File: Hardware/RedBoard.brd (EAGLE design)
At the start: 68.6 x 53.3 mm, 75 parts, among them IC3 LM1117, J1 AMP FCI 10103594-0001LF, J2 ISP, J3 POWER_JACKSUPER_BOMB_DIGITY, Q1 1A/60V/500mΩ, Q2 2N7002PW, Q3 2N7002PW, U1 CH340C, U3 AP2112-3.3V, U4 ATMEGA328P_TQFP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

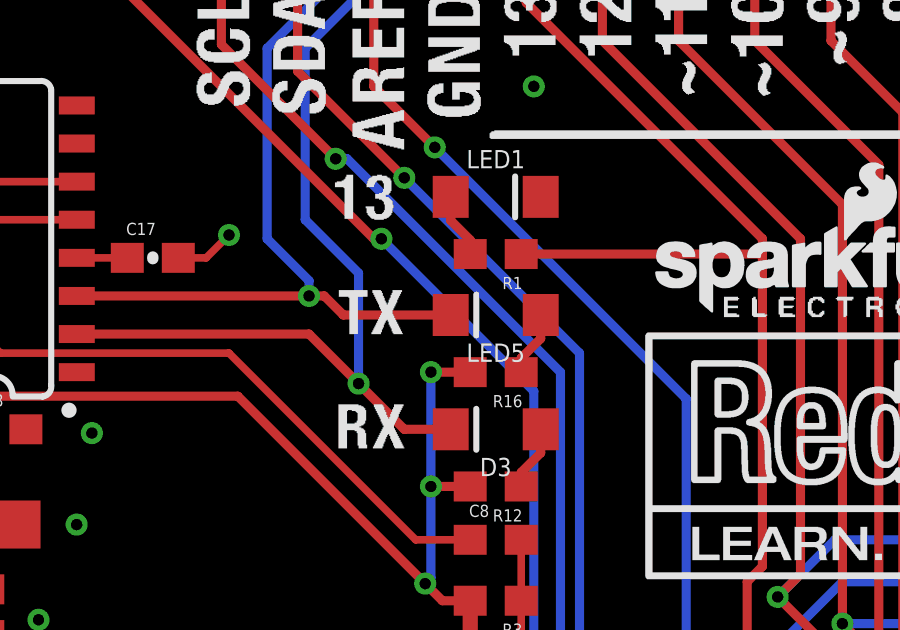
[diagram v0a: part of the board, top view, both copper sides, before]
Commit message: Updated Green TX LED Prod ID
Updated LED5 to Green TX LED Prod ID.
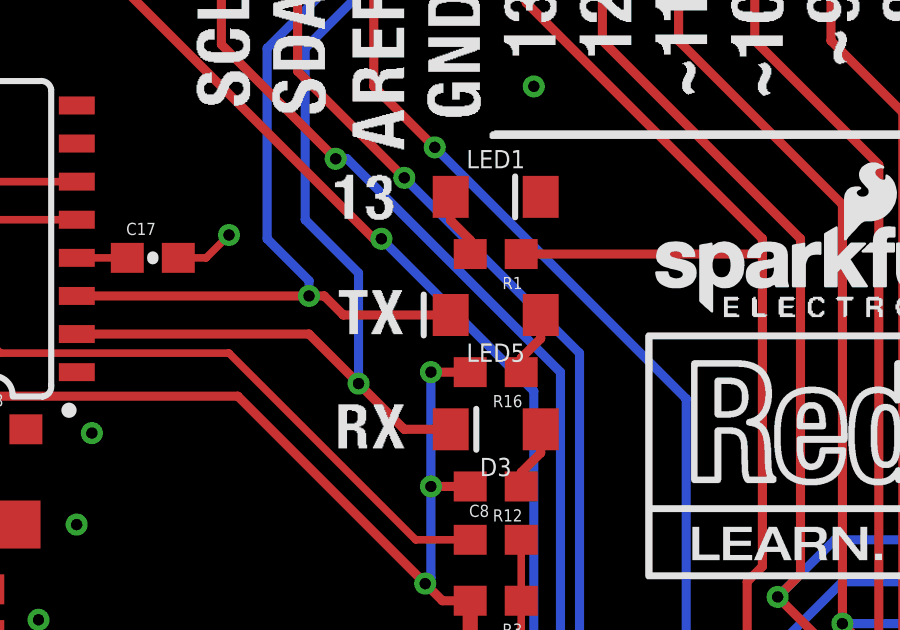
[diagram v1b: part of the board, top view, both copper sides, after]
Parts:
- LED5: device SparkFun-LED:LED-1206-HIDDENSILK -> SparkFun-LED:LED-1206
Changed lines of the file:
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@@
 <?xml version="1.0" encoding="utf-8"?>
 <!DOCTYPE eagle SYSTEM "eagle.dtd">
-<eagle version="9.0.1">
+<eagle version="9.1.3">
 <drawing>
 <settings>
@@
 <param name="checkStop" value="0"/>
 <param name="checkValues" value="0"/>
+<param name="checkNames" value="1"/>
+<param name="checkWireStubs" value="1"/>
+<param name="checkPolygonWidth" value="0"/>
 <param name="useDiameter" value="13"/>
 <param name="maxErrors" value="50"/>
@@
 <attribute name="VALUE" x="-1.016" y="40.894" size="0.508" layer="27" font="vector" rot="R270"/>
 </element>
-<element name="LED5" library="SparkFun-LED" package="LED-1206-HIDDENSILK" value="GREEN" x="27.94" y="36.83" rot="R180">
+<element name="LED5" library="SparkFun-LED" package="LED-1206" value="GREEN" x="27.94" y="36.83" rot="R180">
 <attribute name="NAME" x="27.94" y="35.8775" size="0.6096" layer="25" font="vector" ratio="20" rot="R180" align="bottom-center"/>
-<attribute name="PROD_ID" value="DIO-00862" x="27.94" y="36.83" size="1.778" layer="27" font="vector" ratio="15" rot="R180" display="off"/>
-<attribute name="VALUE" x="31.623" y="36.576" size="0.6096" layer="27" font="vector" ratio="20" rot="R180" align="top-center"/>
+<attribute name="PROD_ID" value="DIO-09910" x="27.94" y="36.83" size="1.778" layer="27" font="vector" ratio="15" rot="R180" display="off"/>
+<attribute name="VALUE" value="GREEN" x="31.623" y="36.576" size="0.6096" layer="27" font="vector" ratio="20" rot="R180" align="top-center"/>
 </element>
 <element name="I/O" library="SparkFun-Jumpers" package="SMT-JUMPER_3_1-NC_TRACE_SILK" value="" x="27.94" y="20.32">
@@
 </signal>
 </signals>
+<mfgpreviewcolors>
+<mfgpreviewcolor name="soldermaskcolor" color="0xC8008000"/>
+<mfgpreviewcolor name="silkscreencolor" color="0xFFFEFEFE"/>
+<mfgpreviewcolor name="backgroundcolor" color="0xFF282828"/>
+<mfgpreviewcolor name="coppercolor" color="0xFFFFBF00"/>
+<mfgpreviewcolor name="substratecolor" color="0xFF786E46"/>
+</mfgpreviewcolors>
 <errors>
 </errors>

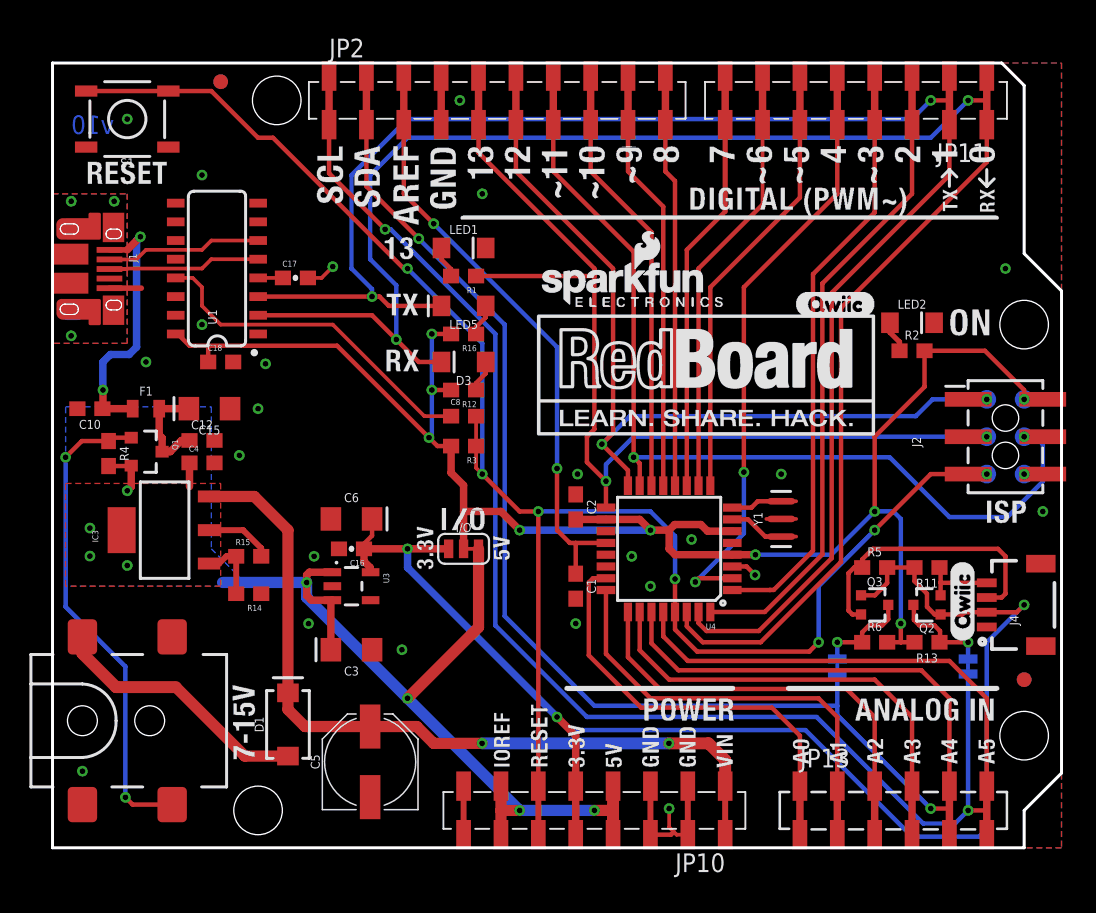
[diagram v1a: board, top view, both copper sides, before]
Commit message: Ch340G with external Oscilator and caps
-Swapped out CH340C for the CH340G
-Added external 12MHz Crystal and caps
-bumped version to v20 in sch and brd
-cleaned up schematic overlap/spacing
-Aprooved DRC errors (wire stubs, dimension and some jumper trace overlaps)
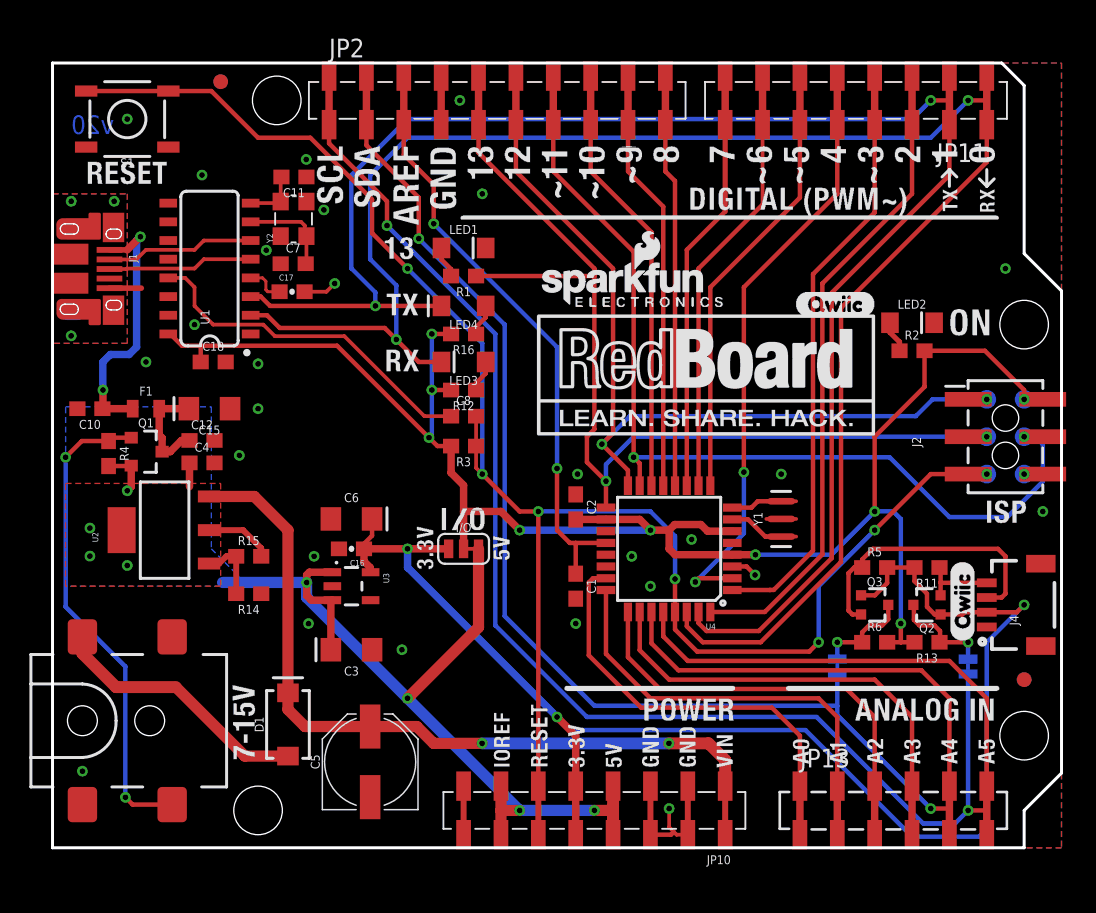
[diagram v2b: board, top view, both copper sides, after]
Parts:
- added C11, C7: 22pF, SparkFun-Capacitors:0603
- added Y2: 12MHz, USB Basic:CRYSTAL-SMD-3.2X2.5
- U1: value CH340C -> CH340G
- U4: value ATMEGA328P_TQFP -> ATMEGA328P
- moved C17 0.97 mm to (16.3, 37.8)
- moved U1 0.51 mm to (10.7, 39.4)
- moved C18 0.51 mm to (10.9, 33.0)
- renumbered D3 to LED3, IC3 to U2, LED5 to LED4
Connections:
- new net N$11: C11.2, U1.8, Y2.3
- new net N$12: C7.2, U1.7, Y2.1
- net GND: now also C11.1, C7.1, Y2.2, Y2.4
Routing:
- net N$12: track 0.00 -> 6.44 mm
- net N$11: track 0.00 -> 3.78 mm
- net RESET: track 119.2 -> 120.6 mm
- net TX-O: track 114.1 -> 115.4 mm
- net N$6: track 1.68 -> 2.69 mm
- net RX-I: track 122.3 -> 122.8 mm
- net N$13: track 10.6 -> 10.1 mm
- net N$14: track 10.4 -> 9.87 mm
- net !DTR: track 23.4 -> 23.9 mm
- net VCC: track 115.5 -> 116.0 mm
- net GND: track 10.4 -> 10.6 mm, vias 25 -> 28
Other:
- board text added: "The Hoff, P. Lewis"
- board text added: "v20"
- board text removed: "The Hoff"
- board text removed: "v10"

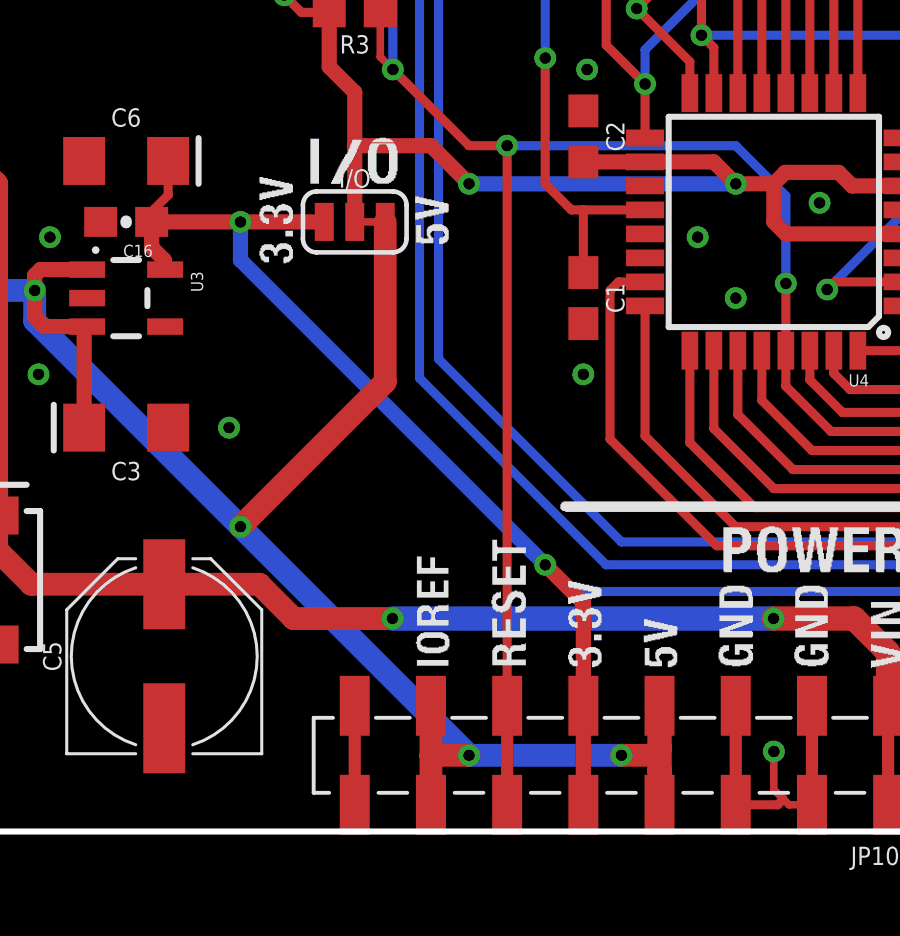
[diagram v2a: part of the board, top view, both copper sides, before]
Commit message: Corrected IOREF Arduino header pin
-This header pin previously was routed to 5V (incorrect), but now it is correctly connected to VCC (aka the logic level of the microcontroller, as selected by "I/O" 3-way jumper).
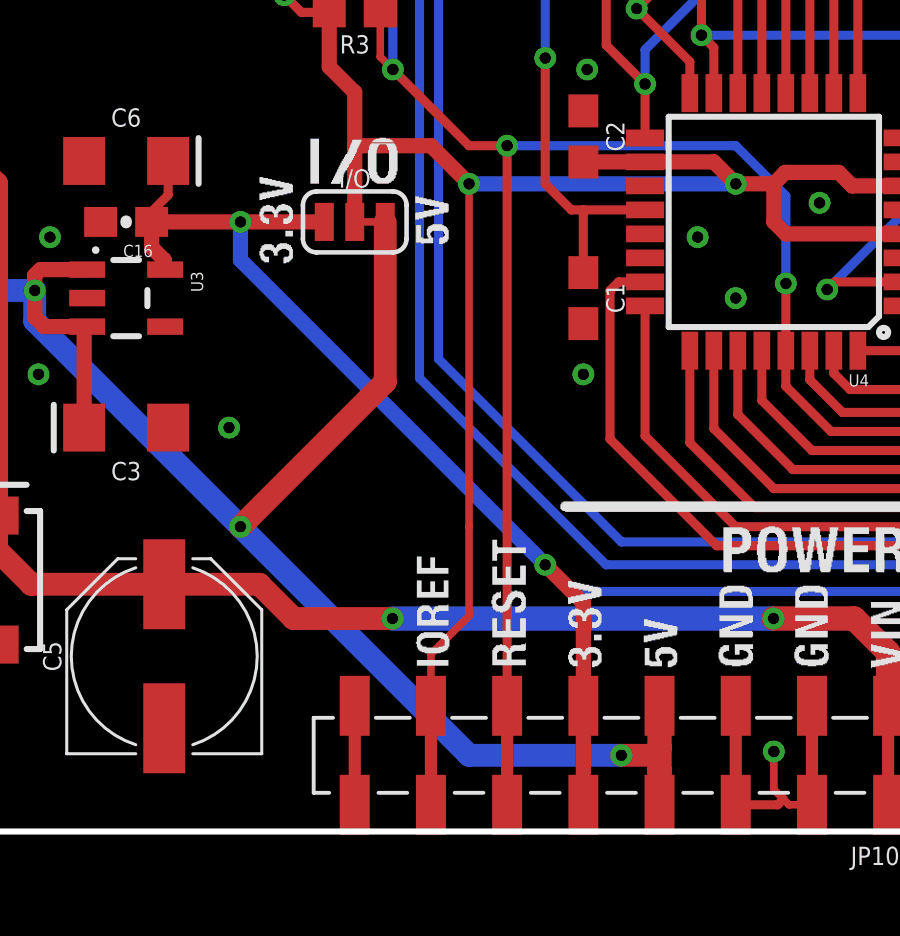
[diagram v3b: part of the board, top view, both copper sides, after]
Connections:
- net 5V: no longer JP10.7
- net VCC: now also JP10.7
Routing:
- net VCC: track 116.0 -> 137.3 mm
- net 5V: track 73.9 -> 69.4 mm, vias 8 -> 7
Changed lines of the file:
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@@
 <contactref element="JP10" pad="4"/>
 <wire x1="38.1" y1="4.19" x2="38.1" y2="2.032" width="0.3048" layer="1"/>
-<contactref element="JP10" pad="7"/>
-<via x="31.75" y="2.54" extent="1-16" drill="0.381"/>
 <wire x1="31.75" y1="2.54" x2="36.83" y2="2.54" width="0.762" layer="16"/>
-<wire x1="31.75" y1="2.54" x2="30.48" y2="2.54" width="0.762" layer="1"/>
-<wire x1="30.48" y1="2.54" x2="30.48" y2="0.89" width="0.762" layer="1"/>
-<wire x1="30.48" y1="4.19" x2="30.48" y2="2.54" width="0.762" layer="1"/>
 <contactref element="R4" pad="2"/>
 <wire x1="17.272" y1="18.034" x2="11.557" y2="18.034" width="0.762" layer="16"/>
@@
 <wire x1="7.868" y1="34.925" x2="8.001" y2="34.925" width="0.3048" layer="1"/>
 <wire x1="8.802" y1="34.124" x2="10.072" y2="34.124" width="0.3048" layer="1"/>
+<contactref element="JP10" pad="7"/>
+<wire x1="31.75" y1="21.59" x2="31.75" y2="10.16" width="0.254" layer="1"/>
+<wire x1="30.48" y1="0.89" x2="30.48" y2="5.9182" width="0.254" layer="1"/>
+<wire x1="31.75" y1="7.1882" x2="31.75" y2="10.16" width="0.254" layer="1"/>
+<wire x1="30.48" y1="5.9182" x2="31.75" y2="7.1882" width="0.254" layer="1"/>
 </signal>
 <signal name="N$13">

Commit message: switched load capacitors to 10pF
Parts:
- C11, C7: value 22pF -> 10pF
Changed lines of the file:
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@@
 <layer number="27" name="tValues" color="7" fill="1" visible="no" active="yes"/>
 <layer number="28" name="bValues" color="7" fill="1" visible="no" active="yes"/>
-<layer number="29" name="tStop" color="2" fill="3" visible="no" active="yes"/>
+<layer number="29" name="tStop" color="2" fill="3" visible="yes" active="yes"/>
 <layer number="30" name="bStop" color="5" fill="6" visible="no" active="yes"/>
-<layer number="31" name="tCream" color="7" fill="4" visible="no" active="yes"/>
+<layer number="31" name="tCream" color="7" fill="4" visible="yes" active="yes"/>
 <layer number="32" name="bCream" color="7" fill="5" visible="no" active="yes"/>
 <layer number="33" name="tFinish" color="6" fill="3" visible="no" active="yes"/>
@@
 <element name="JP15" library="SparkFun" package="FIDUCIAL-1X2" value="FIDUCIAL1X2" x="11.43" y="52.07" smashed="yes" rot="MR0"/>
 <element name="JP16" library="SparkFun" package="FIDUCIAL-1X2" value="FIDUCIAL1X2" x="66.04" y="11.43" smashed="yes" rot="MR0"/>
-<element name="C7" library="SparkFun-Capacitors" package="0603" value="22pF" x="16.3576" y="39.7002" smashed="yes">
+<element name="C7" library="SparkFun-Capacitors" package="0603" value="10pF" x="16.3576" y="39.7002" smashed="yes">
 <attribute name="NAME" x="16.3576" y="40.4622" size="0.6096" layer="25" font="vector" ratio="20" align="bottom-center"/>
-<attribute name="PROD_ID" value="CAP-07876" x="16.3576" y="44.7802" size="1.778" layer="27" display="off"/>
-<attribute name="VALUE" x="16.3576" y="38.9382" size="0.6096" layer="27" font="vector" ratio="20" align="top-center"/>
+<attribute name="PROD_ID" value="CAP-11812" x="16.3576" y="44.7802" size="1.778" layer="27" display="off"/>
+<attribute name="VALUE" value="10pF" x="16.3576" y="38.9382" size="0.6096" layer="27" font="vector" ratio="20" align="top-center"/>
 </element>
-<element name="C11" library="SparkFun-Capacitors" package="0603" value="22pF" x="16.4084" y="45.593" smashed="yes" rot="R180">
+<element name="C11" library="SparkFun-Capacitors" package="0603" value="10pF" x="16.4084" y="45.593" smashed="yes" rot="R180">
 <attribute name="NAME" x="16.4084" y="44.831" size="0.6096" layer="25" font="vector" ratio="20" rot="R180" align="bottom-center"/>
-<attribute name="PROD_ID" value="CAP-07876" x="16.4084" y="40.513" size="1.778" layer="27" rot="R180" display="off"/>
-<attribute name="VALUE" x="16.4084" y="46.355" size="0.6096" layer="27" font="vector" ratio="20" rot="R180" align="top-center"/>
+<attribute name="PROD_ID" value="CAP-11812" x="16.4084" y="40.513" size="1.778" layer="27" rot="R180" display="off"/>
+<attribute name="VALUE" value="10pF" x="16.4084" y="46.355" size="0.6096" layer="27" font="vector" ratio="20" rot="R180" align="top-center"/>
 </element>
 <element name="Y2" library="USB Basic" package="CRYSTAL-SMD-3.2X2.5" value="12MHz" x="16.383" y="42.7482" smashed="yes" rot="R90">
